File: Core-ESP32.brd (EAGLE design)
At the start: 106 x 100 mm, 77 parts, among them Q1 BSS138, Q10 BSS138, Q11 BSS138, Q12 BSS138, Q13 BSS138, Q14 BSS138, Q15 BSS138, Q16 BSS138, Q17 BSS138, Q2 BSS138, Q3 BSS138, Q4 BSS138, Q5 BSS138, Q6 BSS138, Q7 BSS138, Q8 BSS138, Q9 BSS138

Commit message: SPCoast lbr footprint update
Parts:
- moved C2 1.27 mm to (7.62, 67.3)
- moved I2CLED32 1.27 mm to (44.5, 26.7)
- turned LED1 to 0 degrees
- turned Q1 to 270 degrees
- turned Q10 to 270 degrees
- turned Q11 to 270 degrees
- turned Q12 to 270 degrees
- turned Q13 to 270 degrees
- turned Q14 to 270 degrees
- turned Q15 to 0 degrees
- turned Q16 to 0 degrees
- turned Q17 to 0 degrees
- turned Q2 to 270 degrees
- turned Q3 to 270 degrees
- turned Q4 to 270 degrees
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- renumbered FID1 to FID-LR, FID2 to FID-UL
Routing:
- net SDA: track 43.9 -> 46.4 mm
- net +3V3: track 246.3 -> 248.5 mm
- net SCL: track 42.3 -> 43.6 mm
- net +9V: track 243.5 -> 242.2 mm
- net N$1: track 18.1 -> 18.7 mm
- net GND: vias 48 -> 46

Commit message: added values for connectors
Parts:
- CON1, CON2, I2CLED32, I2CLED64, IO-B, IO-C, IO-D, JP2: value (none) -> 0.100
- CON3: value (none) -> 2mm
- J4, J5, J6: value (none) -> RJ12/6
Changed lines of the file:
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@@
 <setting verticaltext="up"/>
 </settings>
-<grid distance="50" unitdist="mil" unit="mil" style="dots" multiple="2" display="yes" altdistance="5" altunitdist="mil" altunit="mil"/>
+<grid distance="50" unitdist="mil" unit="mil" style="dots" multiple="2" display="yes" altdistance="25" altunitdist="mil" altunit="mil"/>
 <layers>
 <layer number="1" name="Top" color="4" fill="1" visible="yes" active="yes"/>
@@
 <attribute name="NAME" x="65.659" y="56.3245" size="1.27" layer="25" font="vector" rot="R180"/>
 </element>
-<element name="J4" library="SPCoast" package="RJ25-INVERTED" value="" x="30.861" y="81.28" smashed="yes" rot="R180">
+<element name="J4" library="SPCoast" package="RJ25-INVERTED" value="RJ12/6" x="30.861" y="81.28" smashed="yes" rot="R180">
 <attribute name="NAME" x="38.481" y="74.676" size="1.27" layer="25" font="vector" rot="R180"/>
 <attribute name="VALUE" x="35.814" y="71.12" size="1.778" layer="27" rot="R180"/>
 </element>
-<element name="IO-B" library="SPCoast" package="1X06_LOCK" value="" x="24.511" y="69.85" smashed="yes">
+<element name="IO-B" library="SPCoast" package="1X06_LOCK" value="0.100" x="24.511" y="69.85" smashed="yes">
 <attribute name="NAME" x="23.241" y="71.628" size="1.27" layer="25" font="vector"/>
 <attribute name="VALUE" x="23.241" y="66.548" size="1.27" layer="27" font="vector"/>
 </element>
-<element name="IO-C" library="SPCoast" package="1X06_LOCK" value="" x="49.276" y="69.85" smashed="yes">
+<element name="IO-C" library="SPCoast" package="1X06_LOCK" value="0.100" x="49.276" y="69.85" smashed="yes">
 <attribute name="NAME" x="48.006" y="71.628" size="1.27" layer="25" font="vector"/>
 <attribute name="VALUE" x="48.006" y="66.548" size="1.27" layer="27" font="vector"/>
 </element>
-<element name="J5" library="SPCoast" package="RJ25-INVERTED" value="" x="55.626" y="81.28" smashed="yes" rot="R180">
+<element name="J5" library="SPCoast" package="RJ25-INVERTED" value="RJ12/6" x="55.626" y="81.28" smashed="yes" rot="R180">
 <attribute name="NAME" x="63.246" y="74.676" size="1.27" layer="25" font="vector" rot="R180"/>
 <attribute name="VALUE" x="60.579" y="71.12" size="1.778" layer="27" rot="R180"/>
 </element>
-<element name="I2CLED32" library="SPCoast" package="1X04_LOCK" value="" x="44.45" y="26.67" smashed="yes" rot="R270">
+<element name="I2CLED32" library="SPCoast" package="1X04_LOCK" value="0.100" x="44.45" y="26.67" smashed="yes" rot="R270">
 <attribute name="NAME" x="52.2732" y="14.0462" size="1.27" layer="25" ratio="10" rot="R180"/>
 <attribute name="VALUE" x="41.275" y="27.94" size="1.27" layer="27" rot="R270"/>
 </element>
-<element name="I2CLED64" library="SPCoast" package="1X04_LOCK" value="" x="65.151" y="30.48" smashed="yes" rot="R180">
+<element name="I2CLED64" library="SPCoast" package="1X04_LOCK" value="0.100" x="65.151" y="30.48" smashed="yes" rot="R180">
 <attribute name="NAME" x="66.8528" y="34.2138" size="1.27" layer="25" ratio="10"/>
 <attribute name="VALUE" x="66.421" y="33.655" size="1.27" layer="27" rot="R180"/>
 </element>
-<element name="J6" library="SPCoast" package="RJ25-INVERTED" value="" x="78.74" y="81.28" smashed="yes" rot="R180">
+<element name="J6" library="SPCoast" package="RJ25-INVERTED" value="RJ12/6" x="78.74" y="81.28" smashed="yes" rot="R180">
 <attribute name="NAME" x="86.36" y="74.676" size="1.27" layer="25" rot="R180"/>
 <attribute name="VALUE" x="83.693" y="71.12" size="1.778" layer="27" rot="R180"/>
@@
 <attribute name="NAME" x="88.773" y="52.5145" size="0.4064" layer="25" rot="R180"/>
 </element>
-<element name="IO-D" library="SPCoast" package="1X06_LOCK" value="" x="72.39" y="69.85"/>
+<element name="IO-D" library="SPCoast" package="1X06_LOCK" value="0.100" x="72.39" y="69.85"/>
 <element name="Q15" library="SPCoast" package="SOT23" value="BSS138" x="15.24" y="29.21" smashed="yes">
 <attribute name="NAME" x="13.335" y="27.305" size="1.27" layer="25" rot="R90"/>
@@
 <attribute name="VALUE" x="13.335" y="22.86" size="0.8128" layer="27" font="vector" rot="R90"/>
 </element>
-<element name="CON1" library="SPCoast" package="1X05_LOCK" value="" x="7.62" y="33.02" smashed="yes" rot="R270">
+<element name="CON1" library="SPCoast" package="1X05_LOCK" value="0.100" x="7.62" y="33.02" smashed="yes" rot="R270">
 <attribute name="NAME" x="5.0038" y="36.1188" size="1.27" layer="25" ratio="10"/>
 <attribute name="VALUE" x="4.445" y="34.29" size="1.27" layer="27" rot="R270"/>
@@
 <element name="LED1" library="SPCoast" package="0603-LED" value="G" x="3.683" y="86.36"/>
 <element name="R35" library="SPCoast" package="0603-RES" value="2k2" x="20.32" y="86.36" rot="R270"/>
-<element name="CON2" library="SPCoast" package="1X04_LOCK" value="" x="90.805" y="34.29" smashed="yes" rot="R90">
+<element name="CON2" library="SPCoast" package="1X04_LOCK" value="0.100" x="90.805" y="34.29" smashed="yes" rot="R90">
 <attribute name="NAME" x="100.4062" y="34.2138" size="0.889" layer="25" ratio="10" rot="R90"/>
 <attribute name="VALUE" x="93.98" y="33.02" size="1.27" layer="27" rot="R90"/>
 </element>
-<element name="CON3" library="SPCoast" package="4P-2.0" value="" x="95.25" y="38.1" smashed="yes" rot="R90">
+<element name="CON3" library="SPCoast" package="4P-2.0" value="2mm" x="95.25" y="38.1" smashed="yes" rot="R90">
 <attribute name="NAME" x="100.33" y="40.005" size="0.889" layer="25" font="vector" ratio="11" rot="R90"/>
 <attribute name="VALUE" x="97.155" y="36.195" size="0.635" layer="27" font="vector" ratio="10" rot="R90"/>
 </element>
-<element name="JP2" library="SPCoast" package="1X03" value="" x="81.28" y="33.02" smashed="yes">
+<element name="JP2" library="SPCoast" package="1X03" value="0.100" x="81.28" y="33.02" smashed="yes">
 <attribute name="NAME" x="101.0412" y="30.4038" size="0.889" layer="25" ratio="10" rot="R90"/>
 <attribute name="VALUE" x="80.01" y="29.845" size="1.27" layer="27"/>

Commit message: added values for connectors
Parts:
- J2: value (none) -> 2.1mm
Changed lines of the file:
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@@
 <attribute name="NAME" x="85.471" y="27.813" size="1.27" layer="25" font="vector" ratio="11" rot="R180"/>
 </element>
-<element name="J2" library="SPCoast" package="DCJ0202" value="" x="31.75" y="22.86" smashed="yes"/>
+<element name="J2" library="SPCoast" package="DCJ0202" value="2.1mm" x="31.75" y="22.86" smashed="yes"/>
 <element name="LABEL1" library="SPCoast" package="PWR_LABEL" value="7.5-12vDC" x="25.4" y="19.05" smashed="yes" rot="R180">
 <attribute name="VALUE" x="22.86" y="23.495" size="1.27" layer="21" font="vector" rot="R270"/>

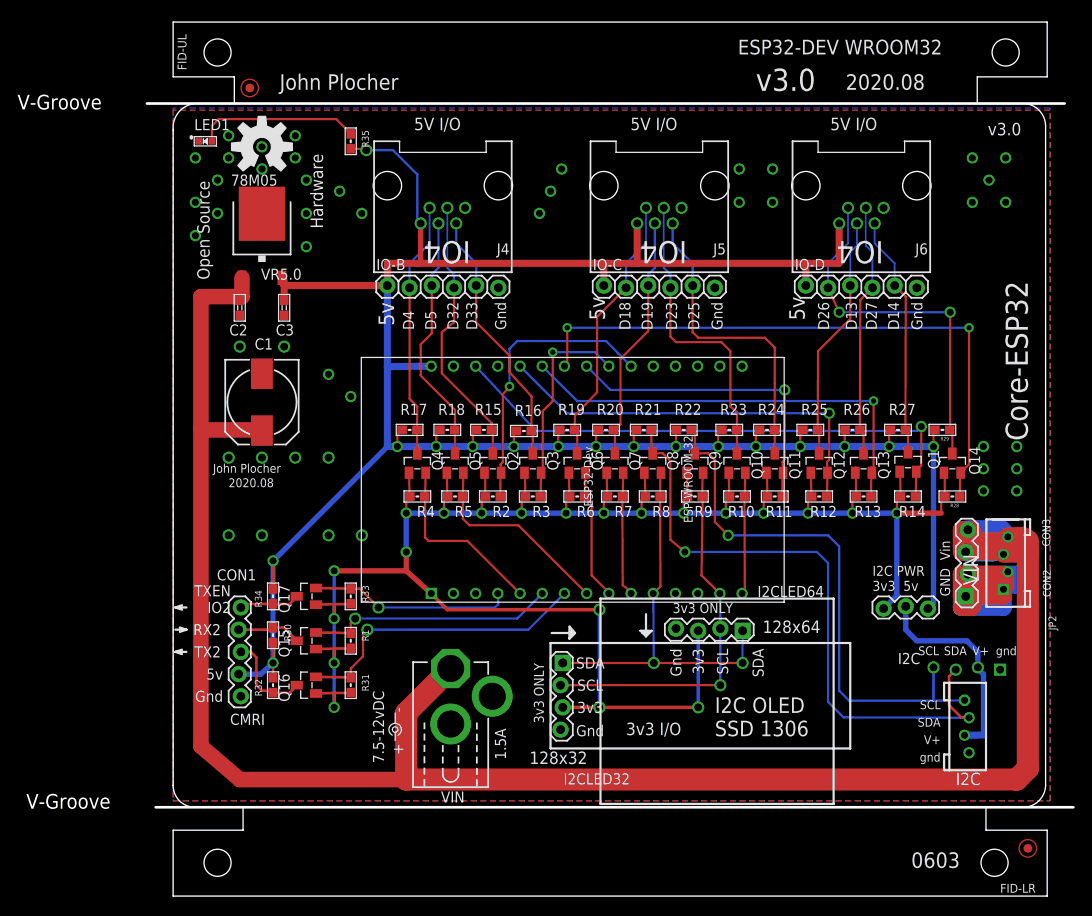
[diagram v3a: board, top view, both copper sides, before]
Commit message: normalized values
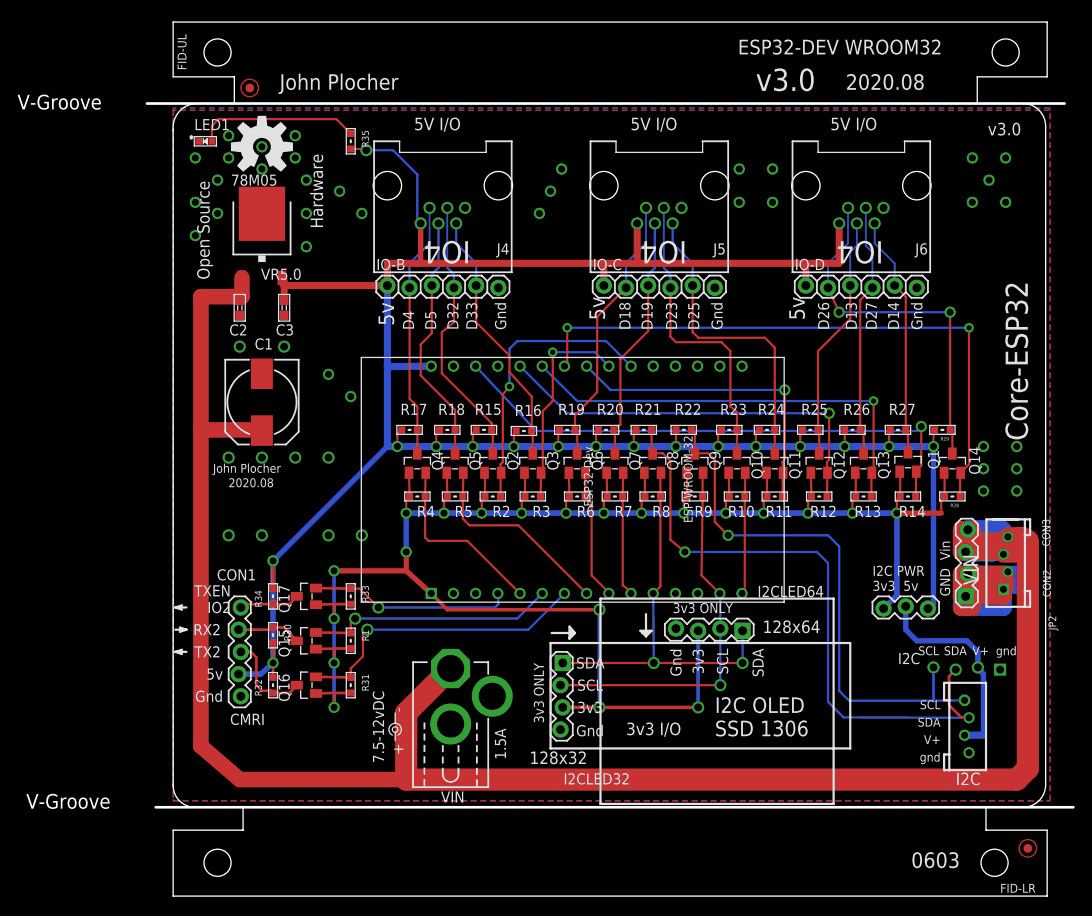
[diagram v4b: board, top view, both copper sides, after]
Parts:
- BOARD: value BOARD80X150 -> BOARD
- C1: value 150uF -> 220uF
- I2C: value CONNECTOR-I2CLEFT -> I2C
- MCU: value ESP32/DEV -> WROOM32
- OSHW1: value OSHW-LOGOL -> OSHW
- VR5.0: value 78M05B -> CJ7805
- renumbered U$1 to MCU
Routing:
- net +3V3: track 248.5 -> 247.8 mm
